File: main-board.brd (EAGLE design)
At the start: 49.2 x 17.8 mm, 56 parts, among them IC1 MEGA328-PB, IC2 MCP73831, IC3 LE33, Q1 3,6864 MHz, Q4 TSM2302CX, T1 IRF7306

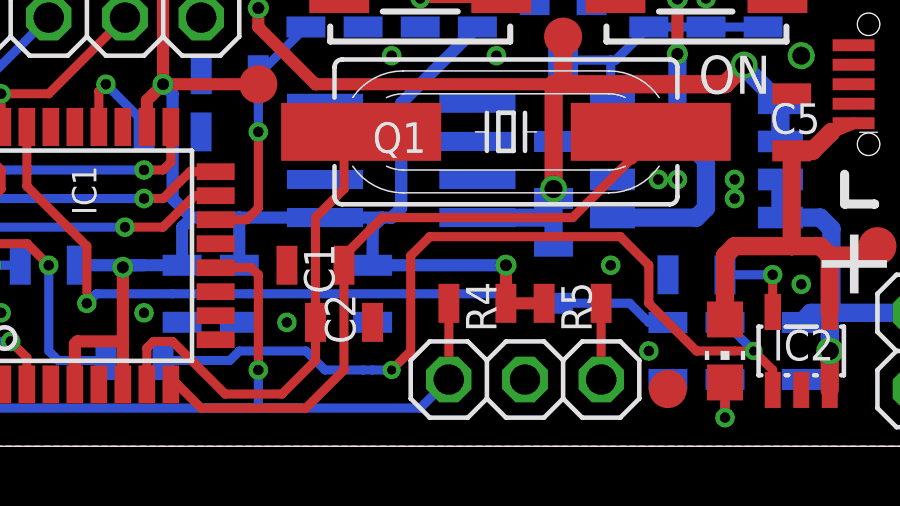
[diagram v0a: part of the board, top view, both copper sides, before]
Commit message: Write meaning of measure signals to silkscreen.
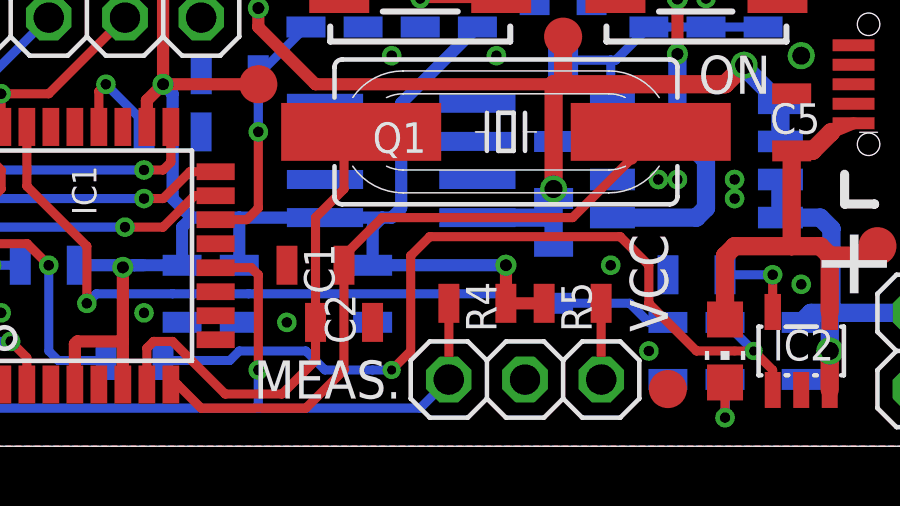
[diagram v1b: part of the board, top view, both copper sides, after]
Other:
- board text added: "MEAS."
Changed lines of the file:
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@@
 <layer number="14" name="Route14" color="1" fill="6" visible="no" active="no"/>
 <layer number="15" name="Route15" color="4" fill="6" visible="no" active="no"/>
-<layer number="16" name="Bottom" color="4" fill="1" visible="yes" active="yes"/>
+<layer number="16" name="Bottom" color="4" fill="1" visible="no" active="yes"/>
 <layer number="17" name="Pads" color="2" fill="1" visible="yes" active="yes"/>
 <layer number="18" name="Vias" color="2" fill="1" visible="yes" active="yes"/>
@@
 <layer number="20" name="Dimension" color="24" fill="1" visible="yes" active="yes"/>
 <layer number="21" name="tPlace" color="7" fill="1" visible="yes" active="yes"/>
-<layer number="22" name="bPlace" color="7" fill="1" visible="yes" active="yes"/>
+<layer number="22" name="bPlace" color="7" fill="1" visible="no" active="yes"/>
 <layer number="23" name="tOrigins" color="15" fill="1" visible="yes" active="yes"/>
-<layer number="24" name="bOrigins" color="15" fill="1" visible="yes" active="yes"/>
-<layer number="25" name="tNames" color="7" fill="1" visible="no" active="yes"/>
+<layer number="24" name="bOrigins" color="15" fill="1" visible="no" active="yes"/>
+<layer number="25" name="tNames" color="7" fill="1" visible="yes" active="yes"/>
 <layer number="26" name="bNames" color="7" fill="1" visible="no" active="yes"/>
 <layer number="27" name="tValues" color="7" fill="1" visible="no" active="yes"/>
@@
 <layer number="44" name="Drills" color="7" fill="1" visible="no" active="yes"/>
 <layer number="45" name="Holes" color="7" fill="1" visible="no" active="yes"/>
-<layer number="46" name="Milling" color="3" fill="1" visible="yes" active="yes"/>
+<layer number="46" name="Milling" color="3" fill="1" visible="no" active="yes"/>
 <layer number="47" name="Measures" color="7" fill="1" visible="no" active="yes"/>
 <layer number="48" name="Document" color="7" fill="1" visible="no" active="yes"/>
-<layer number="49" name="Reference" color="7" fill="1" visible="yes" active="yes"/>
+<layer number="49" name="Reference" color="7" fill="1" visible="no" active="yes"/>
 <layer number="50" name="dxf" color="7" fill="1" visible="no" active="no"/>
 <layer number="51" name="tDocu" color="7" fill="1" visible="yes" active="yes"/>
-<layer number="52" name="bDocu" color="7" fill="1" visible="yes" active="yes"/>
+<layer number="52" name="bDocu" color="7" fill="1" visible="no" active="yes"/>
 <layer number="53" name="tGND_GNDA" color="7" fill="9" visible="no" active="no"/>
 <layer number="54" name="bGND_GNDA" color="1" fill="9" visible="no" active="no"/>
@@
 <text x="48.26" y="10.795" size="1.6764" layer="26" rot="MR270">WSM</text>
 <text x="5.08" y="13.335" size="1.4224" layer="26" rot="MR270">JH 2018</text>
+<text x="29.21" y="2.2225" size="1.27" layer="25" rot="R180" align="center-left">MEAS.</text>
+<text x="38.1" y="3.81" size="1.27" layer="25" rot="R270" align="top-right">VCC</text>
 </plain>
 <attributes>

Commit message: Set R4 to 100k.
The construction of second protoype showed that the value of the pull-up
is critical for proper device function.
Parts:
- R4: value 3K9 -> 100K
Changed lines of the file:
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@@
 <?xml version="1.0" encoding="utf-8"?>
 <!DOCTYPE eagle SYSTEM "eagle.dtd">
-<eagle version="9.0.1">
+<eagle version="9.2.2">
 <drawing>
 <settings>
@@
 <param name="checkStop" value="0"/>
 <param name="checkValues" value="0"/>
+<param name="checkNames" value="1"/>
+<param name="checkWireStubs" value="1"/>
+<param name="checkPolygonWidth" value="0"/>
 <param name="useDiameter" value="13"/>
 <param name="maxErrors" value="50"/>
@@
 <attribute name="NAME" x="8.255" y="11.1125" size="1.27" layer="26" rot="MR0"/>
 </element>
-<element name="R4" library="rcl" package="R0805" value="3K9" x="31.75" y="4.7625" smashed="yes">
+<element name="R4" library="rcl" package="R0805" value="100K" x="31.75" y="4.7625" smashed="yes">
 <attribute name="NAME" x="32.385" y="3.81" size="1.016" layer="25" rot="R90"/>
 <attribute name="VALUE" x="30.1625" y="3.81" size="1.27" layer="27" rot="R90"/>
@@
 </signal>
 </signals>
+<mfgpreviewcolors>
+<mfgpreviewcolor name="soldermaskcolor" color="0xC8008000"/>
+<mfgpreviewcolor name="silkscreencolor" color="0xFFFEFEFE"/>
+<mfgpreviewcolor name="backgroundcolor" color="0xFF282828"/>
+<mfgpreviewcolor name="coppercolor" color="0xFFFFBF00"/>
+<mfgpreviewcolor name="substratecolor" color="0xFF786E46"/>
+</mfgpreviewcolors>
 </board>
 </drawing>
